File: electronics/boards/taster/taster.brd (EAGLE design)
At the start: 48 x 48 mm, 31 parts, among them IC1 ATTINY441-SSU, IC3 NCP1117ST50T3G, J1 GROVE_CONNECTOR2.0_1X4, J2 GROVE_CONNECTOR2.0_1X4, J3 10129383-906001ALF

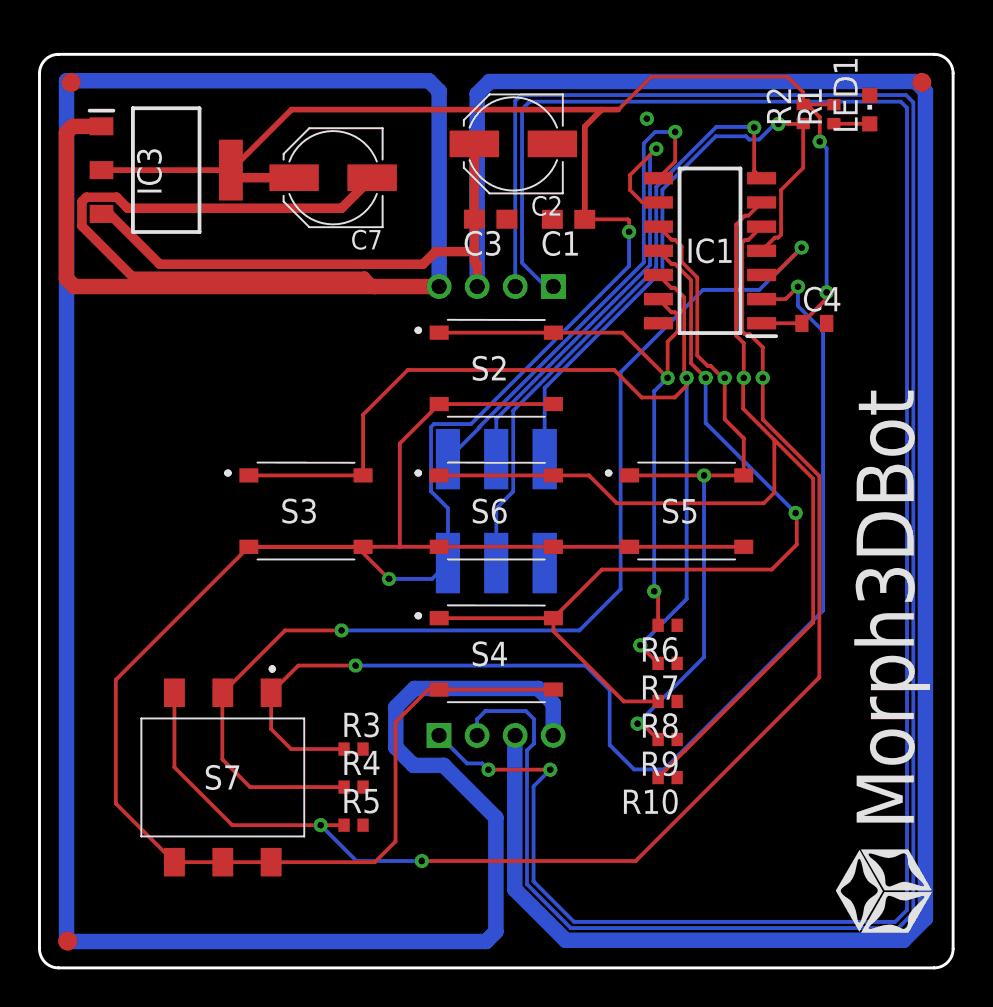
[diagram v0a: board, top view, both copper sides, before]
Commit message: - atmega-Platinen: Stop-Schicht angepasst auf Original - Attiny-Platinen: I2C-Leitungen korrigiert - CAM-Daten für alle Platinen erstellt
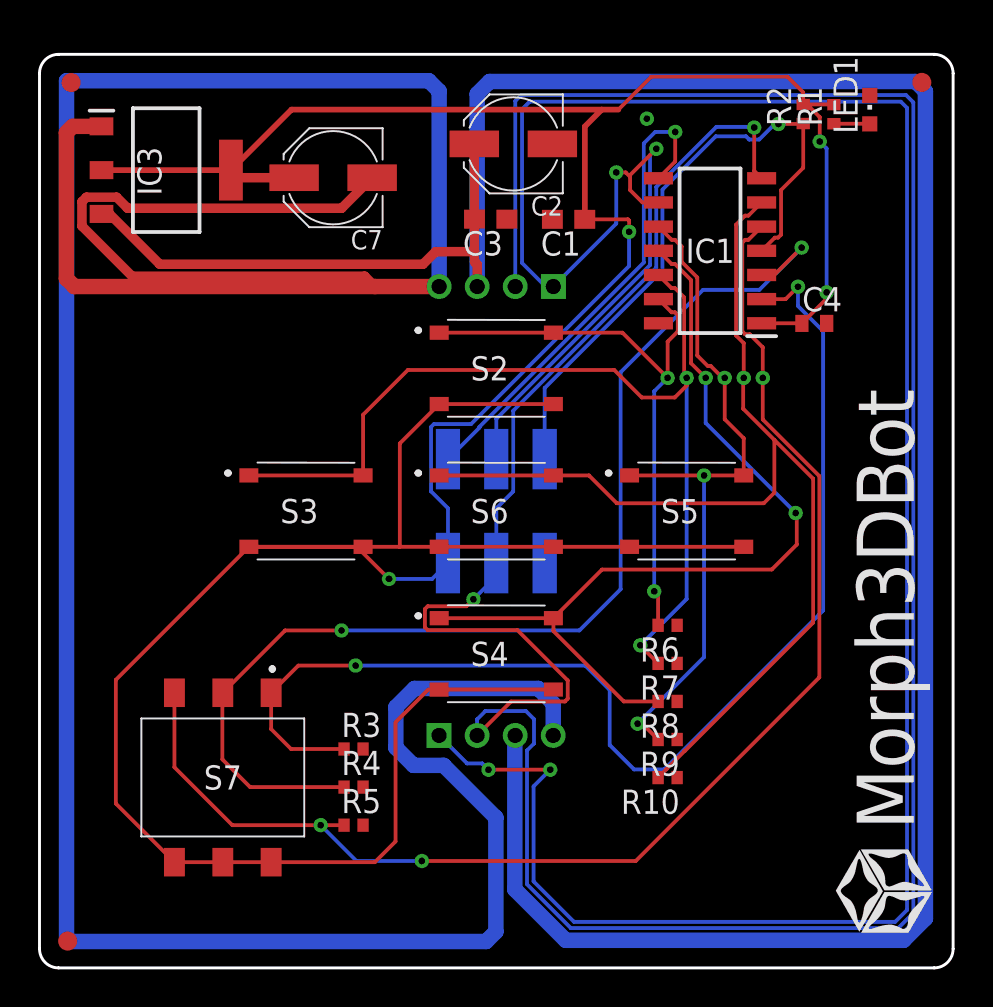
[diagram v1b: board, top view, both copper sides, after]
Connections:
- removed net SCL: J1.1, J2.1
- removed net SDA: J1.2, J2.2
- net MOSI/SDA: now also J1.2, J2.2
- net SCK/SCL: now also J1.1, J2.1
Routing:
- net MOSI/SDA: track 32.6 -> 162.0 mm, vias 1 -> 2
- net SCK/SCL: track 24.3 -> 139.0 mm, vias 1 -> 4
- net SDA: track 108.1 -> 0.00 mm
- net SCL: track 106.5 -> 0.00 mm, vias 2 -> 0
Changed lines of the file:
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@@
 <contactref element="R6" pad="1"/>
-</signal>
-<signal name="SCL">
-<contactref element="J1" pad="1"/>
-<contactref element="J2" pad="1"/>
-<wire x1="20.99033125" y1="12.2144" x2="22.461928125" y2="10.742803125" width="0.2" layer="16"/>
-<wire x1="23.26105625" y1="10.742803125" x2="23.58858125" y2="10.415278125" width="0.2" layer="16"/>
-<via x="23.58858125" y="10.415278125" extent="1-16" drill="0.35"/>
-<via x="26.832009375" y="10.415278125" extent="1-16" drill="0.35"/>
-<wire x1="26.832009375" y1="10.415278125" x2="25.95569375" y2="9.5389625" width="0.2" layer="16"/>
-<wire x1="25.95569375" y1="4.5485625" x2="28.0843625" y2="2.41989375" width="0.2" layer="16"/>
-<wire x1="28.0843625" y1="2.41989375" x2="44.9570875" y2="2.41989375" width="0.2" layer="16"/>
-<wire x1="44.9570875" y1="2.41989375" x2="45.578996875" y2="3.041803125" width="0.2" layer="16"/>
-<wire x1="45.578996875" y1="3.041803125" x2="45.578996875" y2="45.184653125" width="0.2" layer="16"/>
-<wire x1="45.25031875" y1="45.51333125" x2="25.757278125" y2="45.51333125" width="0.2" layer="16"/>
-<wire x1="25.757278125" y1="45.51333125" x2="25.35306875" y2="45.109121875" width="0.2" layer="16"/>
-<wire x1="26.590634375" y1="35.799090625" x2="26.995678125" y2="35.799090625" width="0.2" layer="16"/>
-<wire x1="22.461928125" y1="10.742803125" x2="23.26105625" y2="10.742803125" width="0.2" layer="16"/>
-<wire x1="23.58858125" y1="10.415278125" x2="26.832009375" y2="10.415278125" width="0.2" layer="1"/>
-<wire x1="25.95569375" y1="9.5389625" x2="25.95569375" y2="4.5485625" width="0.2" layer="16"/>
-<wire x1="45.578996875" y1="45.184653125" x2="45.25031875" y2="45.51333125" width="0.2" layer="16"/>
-<wire x1="25.35306875" y1="45.109121875" x2="25.35306875" y2="37.03665625" width="0.2" layer="16"/>
-<wire x1="25.35306875" y1="37.03665625" x2="26.590634375" y2="35.799090625" width="0.2" layer="16"/>
-</signal>
-<signal name="SDA">
-<contactref element="J1" pad="2"/>
-<contactref element="J2" pad="2"/>
-<wire x1="24.995678125" y1="35.799090625" x2="24.995678125" y2="45.54409375" width="0.2" layer="16"/>
-<wire x1="25.310890625" y1="45.85930625" x2="45.526596875" y2="45.85930625" width="0.2" layer="16"/>
-<wire x1="45.526596875" y1="45.85930625" x2="45.909415625" y2="45.4764875" width="0.2" layer="16"/>
-<wire x1="45.909415625" y1="45.4764875" x2="45.909415625" y2="2.881575" width="0.2" layer="16"/>
-<wire x1="45.909415625" y1="2.881575" x2="45.119121875" y2="2.09128125" width="0.2" layer="16"/>
-<wire x1="45.119121875" y1="2.09128125" x2="27.915903125" y2="2.09128125" width="0.2" layer="16"/>
-<wire x1="27.915903125" y1="2.09128125" x2="25.61199375" y2="4.395190625" width="0.2" layer="16"/>
-<wire x1="25.61199375" y1="4.395190625" x2="25.61199375" y2="11.4226875" width="0.2" layer="16"/>
-<wire x1="25.9802" y1="11.79089375" x2="25.9802" y2="13.068228125" width="0.2" layer="16"/>
-<wire x1="25.9802" y1="13.068228125" x2="25.55441875" y2="13.494009375" width="0.2" layer="16"/>
-<wire x1="22.99033125" y1="13.059684375" x2="22.99033125" y2="12.2144" width="0.2" layer="16"/>
-<wire x1="25.61199375" y1="11.4226875" x2="25.9802" y2="11.79089375" width="0.2" layer="16"/>
-<wire x1="25.55441875" y1="13.494009375" x2="23.42465625" y2="13.494009375" width="0.2" layer="16"/>
-<wire x1="23.42465625" y1="13.494009375" x2="22.99033125" y2="13.059684375" width="0.2" layer="16"/>
-<wire x1="24.995678125" y1="45.54409375" x2="25.310890625" y2="45.85930625" width="0.2" layer="16"/>
 </signal>
 <signal name="VCC">
@@
 <wire x1="37.93974375" y1="41.48785625" x2="37.54955625" y2="41.87804375" width="0.2" layer="1"/>
 <wire x1="37.54955625" y1="41.87804375" x2="37.54955625" y2="44.15269375" width="0.2" layer="1"/>
+<contactref element="J1" pad="2"/>
+<contactref element="J2" pad="2"/>
+<wire x1="24.995678125" y1="35.799090625" x2="24.995678125" y2="45.54409375" width="0.2" layer="16"/>
+<wire x1="25.310890625" y1="45.85930625" x2="45.526596875" y2="45.85930625" width="0.2" layer="16"/>
+<wire x1="45.526596875" y1="45.85930625" x2="45.909415625" y2="45.4764875" width="0.2" layer="16"/>
+<wire x1="45.909415625" y1="45.4764875" x2="45.909415625" y2="2.881575" width="0.2" layer="16"/>
+<wire x1="45.909415625" y1="2.881575" x2="45.119121875" y2="2.09128125" width="0.2" layer="16"/>
+<wire x1="45.119121875" y1="2.09128125" x2="27.915903125" y2="2.09128125" width="0.2" layer="16"/>
+<wire x1="27.915903125" y1="2.09128125" x2="25.61199375" y2="4.395190625" width="0.2" layer="16"/>
+<wire x1="25.61199375" y1="4.395190625" x2="25.61199375" y2="11.4226875" width="0.2" layer="16"/>
+<wire x1="25.9802" y1="11.79089375" x2="25.9802" y2="13.068228125" width="0.2" layer="16"/>
+<wire x1="25.9802" y1="13.068228125" x2="25.55441875" y2="13.494009375" width="0.2" layer="16"/>
+<wire x1="22.99033125" y1="13.059684375" x2="22.99033125" y2="12.2144" width="0.2" layer="16"/>
+<wire x1="25.61199375" y1="11.4226875" x2="25.9802" y2="11.79089375" width="0.2" layer="16"/>
+<wire x1="25.55441875" y1="13.494009375" x2="23.42465625" y2="13.494009375" width="0.2" layer="16"/>
+<wire x1="23.42465625" y1="13.494009375" x2="22.99033125" y2="13.059684375" width="0.2" layer="16"/>
+<wire x1="24.995678125" y1="45.54409375" x2="25.310890625" y2="45.85930625" width="0.2" layer="16"/>
+<via x="22.79653125" y="19.369090625" extent="1-16" drill="0.35"/>
+<wire x1="27.60455" y1="13.9976" x2="27.7524" y2="14.14545" width="0.2" layer="1"/>
+<wire x1="27.7524" y1="14.14545" x2="27.7524" y2="15.10455" width="0.2" layer="1"/>
+<wire x1="20.39545" y1="17.7476" x2="20.2476" y2="17.89545" width="0.2" layer="1"/>
+<wire x1="20.2476" y1="17.89545" x2="20.2476" y2="18.85455" width="0.2" layer="1"/>
+<wire x1="20.2476" y1="18.85455" x2="20.39545" y2="19.0024" width="0.2" layer="1"/>
+<wire x1="22.99033125" y1="12.2144" x2="24.77353125" y2="13.9976" width="0.2" layer="1"/>
+<wire x1="24.77353125" y1="13.9976" x2="27.60455" y2="13.9976" width="0.2" layer="1"/>
+<wire x1="27.7524" y1="15.10455" x2="25.10935" y2="17.7476" width="0.2" layer="1"/>
+<wire x1="25.10935" y1="17.7476" x2="20.39545" y2="17.7476" width="0.2" layer="1"/>
+<wire x1="20.39545" y1="19.0024" x2="22.429840625" y2="19.0024" width="0.2" layer="1"/>
+<wire x1="22.429840625" y1="19.0024" x2="22.79653125" y2="19.369090625" width="0.2" layer="1"/>
+<wire x1="22.79653125" y1="19.369090625" x2="24" y2="20.572559375" width="0.2" layer="16"/>
+<wire x1="24" y1="20.572559375" x2="24" y2="21.27" width="0.2" layer="16"/>
 </signal>
 <signal name="SCK/SCL">
@@
 <wire x1="32.51774375" y1="40.21785625" x2="31.676053125" y2="40.21785625" width="0.2" layer="1"/>
 <wire x1="31.676053125" y1="40.21785625" x2="31.028328125" y2="40.86558125" width="0.2" layer="1"/>
-<wire x1="31.028328125" y1="40.86558125" x2="31.028328125" y2="41.658715625" width="0.2" layer="1"/>
+<wire x1="31.028328125" y1="40.86558125" x2="31.028328125" y2="41.56466875" width="0.2" layer="1"/>
+<wire x1="31.028328125" y1="41.56466875" x2="31.028328125" y2="41.658715625" width="0.2" layer="1"/>
 <wire x1="31.028328125" y1="41.658715625" x2="32.405578125" y2="43.035965625" width="0.2" layer="1"/>
+<contactref element="J1" pad="1"/>
+<contactref element="J2" pad="1"/>
+<wire x1="20.99033125" y1="12.2144" x2="22.461928125" y2="10.742803125" width="0.2" layer="16"/>
+<wire x1="23.26105625" y1="10.742803125" x2="23.58858125" y2="10.415278125" width="0.2" layer="16"/>
+<via x="23.58858125" y="10.415278125" extent="1-16" drill="0.35"/>
+<via x="26.832009375" y="10.415278125" extent="1-16" drill="0.35"/>
+<wire x1="26.832009375" y1="10.415278125" x2="25.95569375" y2="9.5389625" width="0.2" layer="16"/>
+<wire x1="25.95569375" y1="4.5485625" x2="28.0843625" y2="2.41989375" width="0.2" layer="16"/>
+<wire x1="28.0843625" y1="2.41989375" x2="44.9570875" y2="2.41989375" width="0.2" layer="16"/>
+<wire x1="44.9570875" y1="2.41989375" x2="45.578996875" y2="3.041803125" width="0.2" layer="16"/>
+<wire x1="45.578996875" y1="3.041803125" x2="45.578996875" y2="45.184653125" width="0.2" layer="16"/>
+<wire x1="45.25031875" y1="45.51333125" x2="25.757278125" y2="45.51333125" width="0.2" layer="16"/>
+<wire x1="25.757278125" y1="45.51333125" x2="25.35306875" y2="45.109121875" width="0.2" layer="16"/>
+<wire x1="26.590634375" y1="35.799090625" x2="26.995678125" y2="35.799090625" width="0.2" layer="16"/>
+<wire x1="22.461928125" y1="10.742803125" x2="23.26105625" y2="10.742803125" width="0.2" layer="16"/>
+<wire x1="23.58858125" y1="10.415278125" x2="26.832009375" y2="10.415278125" width="0.2" layer="1"/>
+<wire x1="25.95569375" y1="9.5389625" x2="25.95569375" y2="4.5485625" width="0.2" layer="16"/>
+<wire x1="45.578996875" y1="45.184653125" x2="45.25031875" y2="45.51333125" width="0.2" layer="16"/>
+<wire x1="25.35306875" y1="45.109121875" x2="25.35306875" y2="37.03665625" width="0.2" layer="16"/>
+<wire x1="25.35306875" y1="37.03665625" x2="26.590634375" y2="35.799090625" width="0.2" layer="16"/>
+<wire x1="26.995678125" y1="35.799090625" x2="30.30215625" y2="39.10556875" width="0.2" layer="16"/>
+<wire x1="30.30215625" y1="39.10556875" x2="30.30215625" y2="41.7952875" width="0.2" layer="16"/>
+<via x="30.30215625" y="41.7952875" extent="1-16" drill="0.35"/>
+<wire x1="30.30215625" y1="41.7952875" x2="30.797709375" y2="41.7952875" width="0.2" layer="1"/>
+<wire x1="30.797709375" y1="41.7952875" x2="31.028328125" y2="41.56466875" width="0.2" layer="1"/>
 </signal>
 <signal name="RESET">
